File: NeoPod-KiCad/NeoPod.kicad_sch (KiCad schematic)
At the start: 3 parts, among them U1 ESP32-WROOM-32, U2 PCM5102A

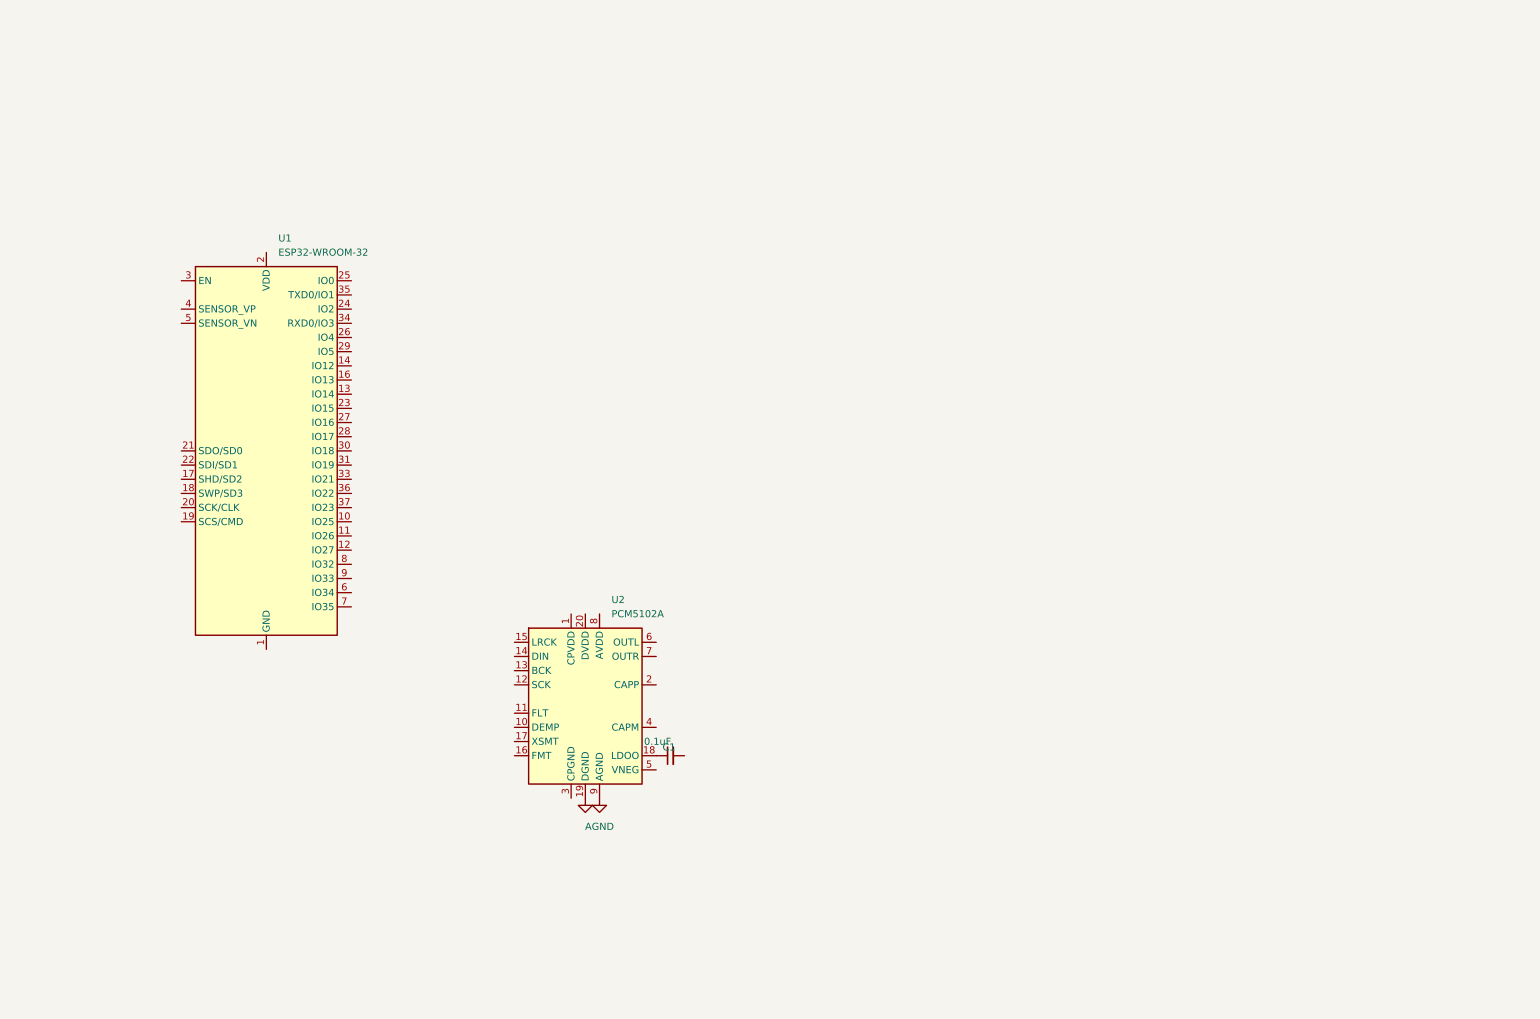
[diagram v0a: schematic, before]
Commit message: finished schematic and added picture of finished schematic
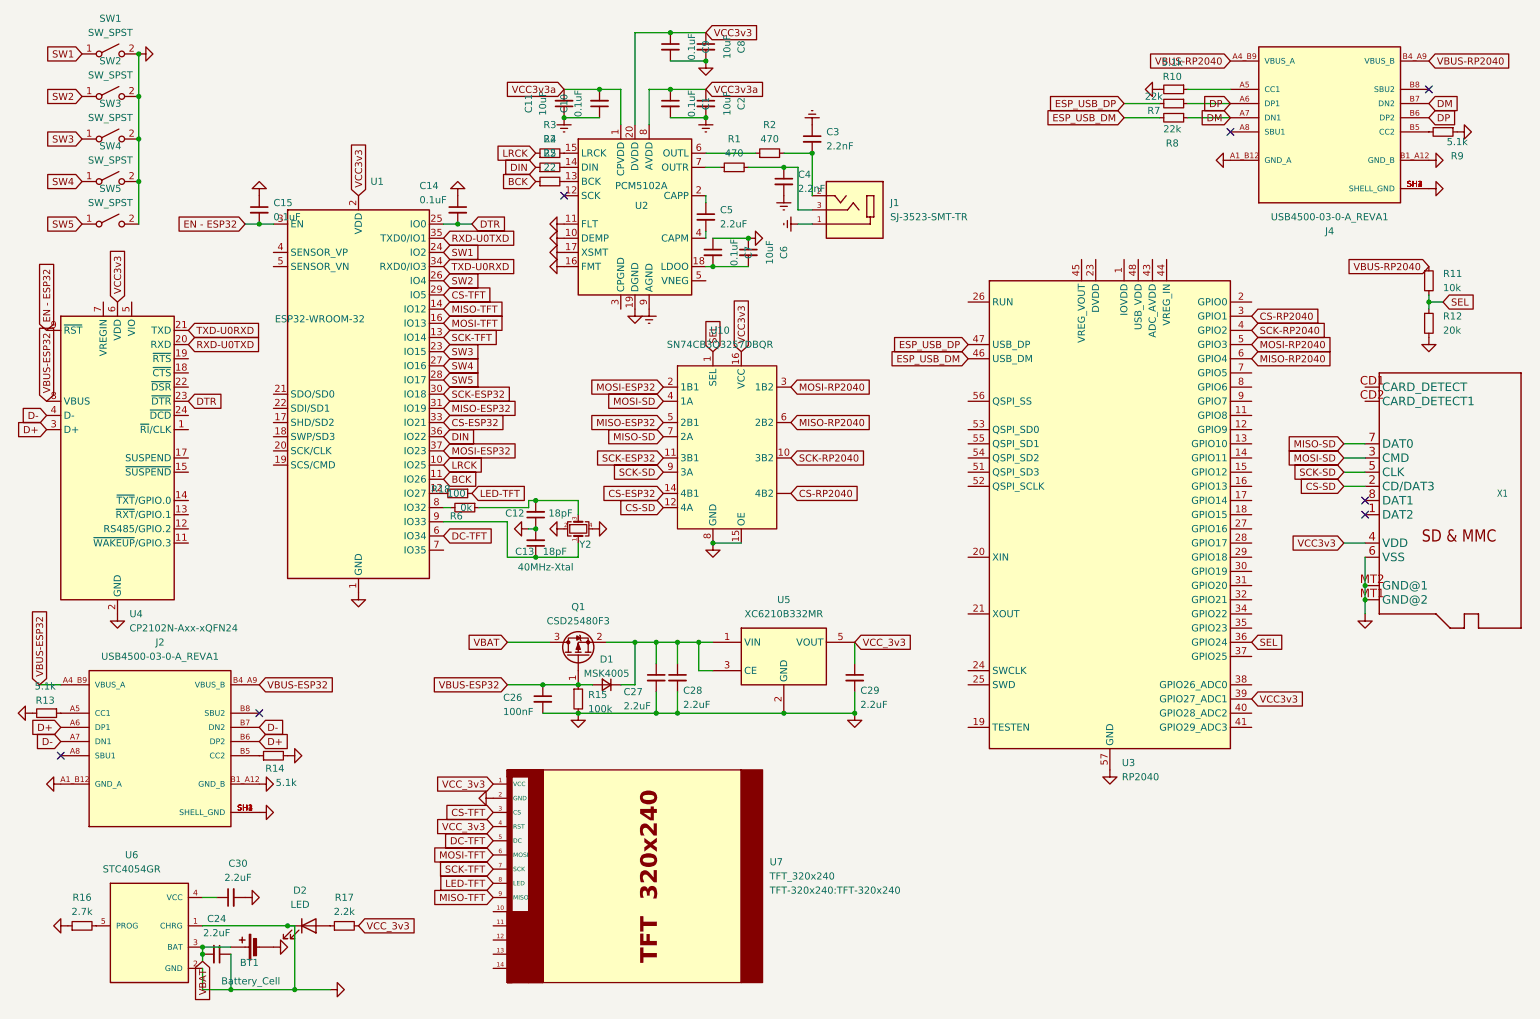
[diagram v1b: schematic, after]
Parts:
- added BT1: Battery_Cell, Connector_JST:JST_PH_S2B-PH-SM4-TB_1x02-1MP_P2.00mm_Horizontal, symbol Device:Battery_Cell
- added C10, C14, C15, C7, C9: 0.1uF, Capacitor_SMD:C_0603_1608Metric, symbol Device:C_Small
- added C11, C2, C6, C8: 10uF, Capacitor_SMD:C_0402_1005Metric, symbol Device:C_Small
- added C12, C13: 18pF, Capacitor_SMD:C_0603_1608Metric, symbol Device:C_Small
- added C24, C27, C28, C29, C30, C5: 2.2uF, Capacitor_SMD:C_0603_1608Metric, symbol Device:C_Small
- added C26: 100nF, Capacitor_SMD:C_0402_1005Metric, symbol Device:C_Small
- added C3, C4: 2.2nF, Capacitor_SMD:C_0603_1608Metric, symbol Device:C_Small
- added D1: MSK4005, Diode_SMD:D_SOD-523, symbol Device:D_Small
- added D2: LED, LED_SMD:LED_0603_1608Metric, symbol Device:LED
- added J1: SJ-3523-SMT-TR, Connector_Audio:Jack_3.5mm_CUI_SJ-3523-SMT_Horizontal, symbol SJ-3523-SMT-TR:SJ-3523-SMT-TR
- added J2, J4: USB4500-03-0-A_REVA1, USB-C-2.0-24P(16+8):GCT_USB4500-03-0-A_REVA1, symbol USB-C-2.0-24P(16+8):USB4500-03-0-A_REVA1
- added Q1: CSD25480F3, Package_DFN_QFN:Texas_PicoStar_DFN-3_0.69x0.60mm, symbol Transistor_FET:CSD25480F3
- added R1, R2: 470, Resistor_SMD:R_0603_1608Metric, symbol Device:R_Small
- added R10, R13, R14, R9: 5.1k, Resistor_SMD:R_0603_1608Metric, symbol Device:R_Small
- added R11: 10k, Resistor_SMD:R_0603_1608Metric, symbol Device:R_Small
- added R12: 20k, Resistor_SMD:R_0603_1608Metric, symbol Device:R_Small
- added R15: 100k, Resistor_SMD:R_0402_1005Metric, symbol Device:R_Small
- added R16: 2.7k, Resistor_SMD:R_0603_1608Metric, symbol Device:R_Small
- added R17: 2.2k, Resistor_SMD:R_0603_1608Metric, symbol Device:R_Small
- added R18: 100, Resistor_SMD:R_0402_1005Metric, symbol Device:R_Small
- added R3, R4, R5: 22, Resistor_SMD:R_0402_1005Metric, symbol Device:R_Small
- added R6: 0k, Resistor_SMD:R_0402_1005Metric, symbol Device:R_Small
- added R7, R8: 22k, Resistor_SMD:R_0603_1608Metric, symbol Device:R_Small
- added SW1, SW2, SW3, SW4, SW5: SW_SPST, Kailh_Choc_White:Choc_V1, symbol Switch:SW_SPST
- added U10: SN74CB3Q3257DBQR, SN74CB3Q3257DBQR:SN74CB3Q3257DBQR, symbol SN74CB3Q3257DBQR:SN74CB3Q3257DBQR
- added U3: RP2040, Package_DFN_QFN:QFN-56-1EP_7x7mm_P0.4mm_EP3.2x3.2mm, symbol MCU_RaspberryPi:RP2040
- added U4: CP2102N-Axx-xQFN24, Package_DFN_QFN:QFN-24-1EP_4x4mm_P0.5mm_EP2.6x2.6mm, symbol Interface_USB:CP2102N-Axx-xQFN24
- added U5: XC6210B332MR, Package_TO_SOT_SMD:SOT-23-5, symbol Regulator_Linear:XC6210B332MR
- added U6: STC4054GR, STC4054GR:SOT95P280X110-5N, symbol STC4054GR:STC4054GR
- added U7: TFT_320x240, TFT-320x240:TFT-320x240, symbol TFT_320x240:TFT_320x240
- added X1: ~, Adafruit_MicroSD_Socket:MicroSD_Socket, symbol Adafruit_microSD:MICROSD
- added Y2: 40MHz-Xtal, Crystal:Crystal_SMD_3225-4Pin_3.2x2.5mm, symbol Device:Crystal_GND24_Small
- C1: footprint (none) -> Capacitor_SMD:C_0603_1608Metric
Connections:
- net AGND: now also U1.1 (GND), U1.15 (GND), U1.38 (GND), U1.39 (GND), U2.10 (DEMP), U2.11 (FLT), U2.16 (FMT), U2.17 (XSMT), U2.19 (DGND), C14.1, C15.1, C6.1, C7.1, C8.2, C9.2, J2.A1_B12 (GND_A), J2.B1_A12 (GND_B), J2.SH1 (SHELL_GND), J2.SH2 (SHELL_GND), J2.SH3 (SHELL_GND), J2.SH4 (SHELL_GND), R12.2, SW1.2 (B), SW2.2 (B), SW3.2 (B), SW4.2 (B), SW5.2 (B), U3.57 (GND), U4.2 (GND), U4.25 (GND); no longer U2.9 (AGND)
- net GND: now also BT1.2 (-), C12.1, C13.2, C24.1, C26.2, C27.2, C28.2, C29.2, C30.2, D2.1 (K), J4.A1_B12 (GND_A), J4.B1_A12 (GND_B), J4.SH1 (SHELL_GND), J4.SH2 (SHELL_GND), J4.SH3 (SHELL_GND), J4.SH4 (SHELL_GND), R10.2, R13.2, R14.2, R15.2, R16.1, R9.1, U10.15 (OE), U10.8 (GND), U5.2 (GND), U6.1 (CHRG), U6.2 (GND), U7.2 (GND), X1.6 (VSS), X1.MT1 (GND@2), X1.MT2 (GND@1), Y2.2, Y2.4; no longer U2.19 (DGND)
- net VCC3v3a: now reaches U2.1 (CPVDD)
- net VCC3v3a: now also C1.1, U2.8 (AVDD), C10.2, C11.2, C2.1
- net at U2.13 (BCK): now also R5.2
- net at U2.14 (DIN): now also R4.2
- net at U2.15 (LRCK): now also R3.2
- net at U2.18 (LDOO): now also C6.2, C7.2; no longer C1.1
- net at U2.2 (CAPP): now also C5.1
- net VCC3v3: now reaches U2.20 (DVDD)
- net VCC3v3: now also U1.2 (VDD), C8.1, C9.1, U10.16 (VCC), U3.39 (GPIO27_ADC1), U4.6 (VDD), X1.4 (VDD)
- net at U2.4 (CAPM): now also C5.2
- net at U2.6 (OUTL): now also R2.1
- net at U2.7 (OUTR): now also R1.1
- net LRCK: now reaches U1.10 (IO25)
- net LRCK: now also R3.1
- net BCK: now reaches U1.11 (IO26)
- net BCK: now also R5.1
- net at U1.12 (IO27): now also R18.2
- net SCK-TFT: now reaches U1.13 (IO14)
- net SCK-TFT: now also U7.7 (SCK)
- net MISO-TFT: now reaches U1.14 (IO12)
- net MISO-TFT: now also U7.9 (MISO)
- net MOSI-TFT: now reaches U1.16 (IO13)
- net MOSI-TFT: now also U7.6 (MOSI)
- net SW3: now reaches U1.23 (IO15)
- net SW3: now also SW3.1 (A)
- net SW1: now reaches U1.24 (IO2)
- net SW1: now also SW1.1 (A)
- net DTR: now reaches U1.25 (IO0)
- net DTR: now also C14.2, U4.23 (~{DTR})
- net SW2: now reaches U1.26 (IO4)
- net SW2: now also SW2.1 (A)
- net SW4: now reaches U1.27 (IO16)
- net SW4: now also SW4.1 (A)
- net SW5: now reaches U1.28 (IO17)
- net SW5: now also SW5.1 (A)
- net CS-TFT: now reaches U1.29 (IO5)
- net CS-TFT: now also U7.3 (CS)
- net EN - ESP32: now reaches U1.3 (EN)
- net EN - ESP32: now also C15.2, U4.9 (~{RST})
- net SCK-ESP32: now reaches U1.30 (IO18)
- net SCK-ESP32: now also U10.11 (3B1)
- net MISO-ESP32: now reaches U1.31 (IO19)
- net MISO-ESP32: now also U10.5 (2B1)
- net CS-ESP32: now reaches U1.33 (IO21)
- net CS-ESP32: now also U10.14 (4B1)
- net TXD-U0RXD: now reaches U1.34 (RXD0/IO3)
- net TXD-U0RXD: now also U4.21 (TXD)
- net RXD-U0TXD: now reaches U1.35 (TXD0/IO1)
- net RXD-U0TXD: now also U4.20 (RXD)
- net DIN: now reaches U1.36 (IO22)
- net DIN: now also R4.1
- net MOSI-ESP32: now reaches U1.37 (IO23)
- net MOSI-ESP32: now also U10.2 (1B1)
- net DC-TFT: now reaches U1.6 (IO34)
- net DC-TFT: now also U7.5 (DC)
- net at U1.8 (IO32): now also R6.2
- net at U1.9 (IO33): now also C13.1, Y2.1
- net GNDREF: now reaches C1.2
- net GNDREF: now also U2.9 (AGND), C10.1, C11.1, C2.2, C3.1, C4.2, J1.1
- new net: C27.1, C28.1, D1.1 (K), Q1.2 (S), U5.1 (VIN), U5.3 (CE)
- new net: J2.A5 (CC1), R13.1
- new net: J4.A5 (CC1), R10.1
- new net: C30.1, U6.4 (VCC)
- new net: D2.2 (A), R17.1
- new net: J4.B5 (CC2), R9.2
- new net: C3.2, J1.2, R2.2
- new net: C4.1, J1.3, R1.2
- new net: C12.2, R6.1, Y2.3
- new net: U3.1 (IOVDD), U3.10 (IOVDD), U3.22 (IOVDD), U3.33 (IOVDD), U3.42 (IOVDD), U3.49 (IOVDD)
- new net: U3.23 (DVDD), U3.50 (DVDD)
- new net: R16.2, U6.5 (PROG)
- new net: J2.B5 (CC2), R14.1
- new net CS-RP2040: U10. (4B2), U3.3 (GPIO1)
- new net CS-SD: U10.12 (4A), X1.2 (CD/DAT3)
- new net D+: J2.A6 (DP1), J2.B6 (DP2), U4.3 (D+)
- new net D-: J2.A7 (DN1), J2.B7 (DN2), U4.4 (D-)
- new net DM: J4.A7 (DN1), J4.B7 (DN2), R8.1
- new net DP: J4.A6 (DP1), J4.B6 (DP2), R7.1
- new net ESP_USB_DM: R8.2, U3.46 (USB_DM)
- new net ESP_USB_DP: R7.2, U3.47 (USB_DP)
- new net LED-TFT: R18.1, U7.8 (LED)
- new net MISO-RP2040: U10.6 (2B2), U3.6 (GPIO4)
- new net MISO-SD: U10.7 (2A), X1.7 (DAT0)
- new net MOSI-RP2040: U10.3 (1B2), U3.5 (GPIO3)
- new net MOSI-SD: U10.4 (1A), X1.3 (CMD)
- new net SCK-RP2040: U10.10 (3B2), U3.4 (GPIO2)
- new net SCK-SD: U10.9 (3A), X1.5 (CLK)
- new net SEL: R11.2, R12.1, U10.1 (SEL), U3.36 (GPIO24)
- new net VBAT: BT1.1 (+), C24.2, Q1.3 (D), U6.3 (BAT)
- new net VBUS-ESP32: C26.1, D1.2 (A), J2.A4_B9 (VBUS_A), J2.B4_A9 (VBUS_B), Q1.1 (G), R15.1, U4.8 (VBUS)
- new net VBUS-RP2040: J4.A4_B9 (VBUS_A), J4.B4_A9 (VBUS_B), R11.1
- new net VCC_3v3: C29.1, R17.2, U5.5 (VOUT), U7.1 (VCC), U7.4 (RST)
- no-connect marks 0 -> 7
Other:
- moved on the sheet: U1, U2
